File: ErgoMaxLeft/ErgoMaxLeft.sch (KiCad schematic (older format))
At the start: 92 parts, among them J1 AudioJack4_Ground, K1 KEYSW, K10 KEYSW, K11 KEYSW, K12 KEYSW, K13 KEYSW, K14 KEYSW, K15 KEYSW, K16 KEYSW, K17 KEYSW, K18 KEYSW, K19 KEYSW, K2 KEYSW, K20 KEYSW, K21 KEYSW, K22 KEYSW, K23 KEYSW, K24 KEYSW, K25 KEYSW, K26 KEYSW, K27 KEYSW, K28 KEYSW, K29 KEYSW, K3 KEYSW, K30 KEYSW, K31 KEYSW, K32 KEYSW, K33 KEYSW, K34 KEYSW, K35 KEYSW, K36 KEYSW, K37 KEYSW, K38 KEYSW, K39 KEYSW, K4 KEYSW, K40 KEYSW, K41 KEYSW, K42 KEYSW, K43 KEYSW, K44 KEYSW, K5 KEYSW, K6 KEYSW, K7 KEYSW, K8 KEYSW, K9 KEYSW, U1 ProMicro

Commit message: WIP PCB - update diodes footprints to something more accurate, displayed in the proper direction
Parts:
- D1, D10, D11, D12, D13, D14, D15, D16, D17, D18, D19, D2, D20, D21, D22, D23, D24, D25, D26, D27, D28, D29, D3, D30, D31, D32, D33, D34, D35, D36, D37, D38, D39, D4, D40, D41, D42, D43, D44, D5, D6, D7, D8, D9: footprint Keebio-Parts:Diode -> Keebio-Parts:Diode_Long
- J1: footprint Keebio-Parts:4pin35mmAudio -> keyboard_parts:4pin35mmAudio

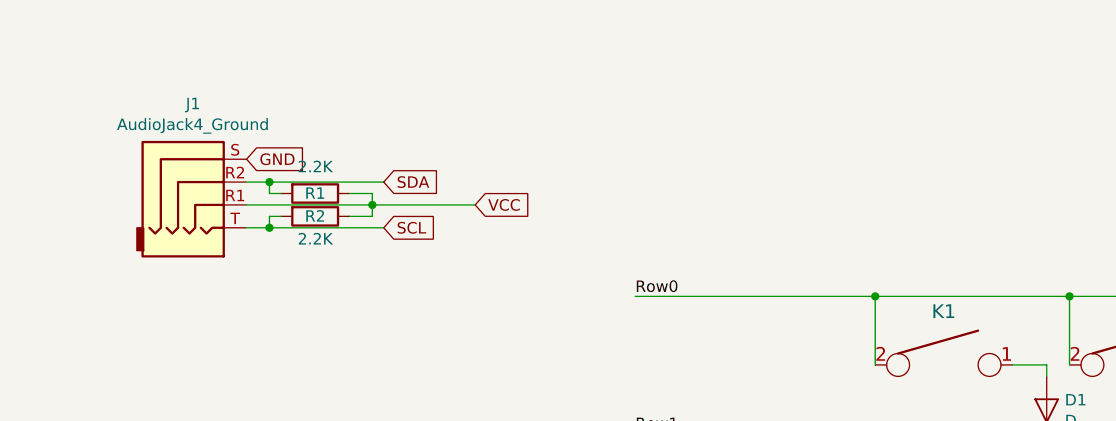
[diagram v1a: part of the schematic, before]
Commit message: WIP PCB - replace jack connector in schematics and PCB to something that actually works properly
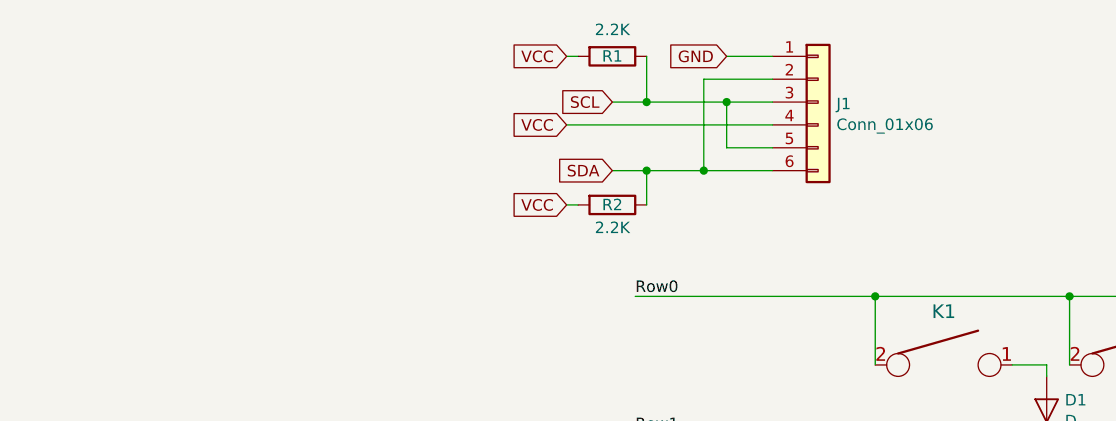
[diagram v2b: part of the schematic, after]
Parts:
- removed J1: AudioJack4_Ground, keyboard_parts:4pin35mmAudio, symbol Connector:AudioJack4_Ground
- added J1: Conn_01x06, Keebio-Parts:4pin35mmAudio, symbol Connector_Generic:Conn_01x06
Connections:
- net GND: now also J1.1 (Pin_1)
- net SCL: now also R1.1, J1.3 (Pin_3), J1.5 (Pin_5); no longer R2.2
- net SDA: now also R2.1, J1.2 (Pin_2), J1.6 (Pin_6); no longer R1.2
- net VCC: now also R1.2, R2.2, J1.4 (Pin_4); no longer R1.1, R2.1
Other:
- moved on the sheet: R1, R2
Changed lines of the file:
@@
-$EndComp
-$Comp
-L Connector:AudioJack4_Ground J1
-U 1 1 5BE696F3
-P 1750 1250
-F 0 "J1" H 1716 1592 50  0000 C CNN
-F 1 "AudioJack4_Ground" H 1716 1501 50  0000 C CNN
-F 2 "keyboard_parts:4pin35mmAudio" H 1750 1250 50  0001 C CNN
-F 3 "~" H 1750 1250 50  0001 C CNN
-	1    1750 1250
-	1    0    0    -1
 $EndComp
 $Comp
@@
 Text GLabel 2650 2750 2    50   Input ~ 0
 GND
-Text GLabel 1950 1150 2    50   Input ~ 0
-GND
 Text GLabel 2650 2950 2    50   Input ~ 0
-VCC
-Text GLabel 2950 1350 2    50   Input ~ 0
 VCC
 Text GLabel 1250 3050 0    50   Input ~ 0
 SDA
-Text GLabel 2550 1250 2    50   Input ~ 0
-SDA
 Text GLabel 1250 3150 0    50   Input ~ 0
 SCL
-Text GLabel 2550 1450 2    50   Input ~ 0
-SCL
 $Comp
 L Device:R R1
 U 1 1 5C270960
-P 2250 1300
-F 0 "R1" V 2250 1300 50  0000 C CNN
-F 1 "2.2K" V 2134 1300 50  0000 C CNN
-F 2 "Keebio-Parts:Resistor" V 2180 1300 50  0001 C CNN
-F 3 "~" H 2250 1300 50  0001 C CNN
-	1    2250 1300
+P 3550 700
+F 0 "R1" V 3550 700 50  0000 C CNN
+F 1 "2.2K" V 3434 700 50  0000 C CNN
+F 2 "Keebio-Parts:Resistor" V 3480 700 50  0001 C CNN
+F 3 "~" H 3550 700 50  0001 C CNN
+	1    3550 700
 	0    1    1    0
 $EndComp
@@
 L Device:R R2
 U 1 1 5C270B6B
-P 2250 1400
-F 0 "R2" V 2250 1400 50  0000 C CNN
-F 1 "2.2K" V 2350 1400 50  0000 C CNN
-F 2 "Keebio-Parts:Resistor" V 2180 1400 50  0001 C CNN
-F 3 "~" H 2250 1400 50  0001 C CNN
-	1    2250 1400
+P 3550 1350
+F 0 "R2" V 3550 1350 50  0000 C CNN
+F 1 "2.2K" V 3650 1350 50  0000 C CNN
+F 2 "Keebio-Parts:Resistor" V 3480 1350 50  0001 C CNN
+F 3 "~" H 3550 1350 50  0001 C CNN
+	1    3550 1350
 	0    1    1    0
 $EndComp
-Wire Wire Line
-	2550 1250 2050 1250
-Wire Wire Line
-	2550 1450 2050 1450
-Wire Wire Line
-	2950 1350 2500 1350
-Wire Wire Line
-	2500 1350 2500 1300
-Wire Wire Line
-	2500 1300 2400 1300
-Connection ~ 2500 1350
-Wire Wire Line
-	2500 1350 1950 1350
-Wire Wire Line
-	2100 1300 2050 1300
-Wire Wire Line
-	2050 1300 2050 1250
-Connection ~ 2050 1250
-Wire Wire Line
-	2050 1250 1950 1250
-Wire Wire Line
-	2400 1400 2500 1400
-Wire Wire Line
-	2500 1400 2500 1350
-Wire Wire Line
-	2100 1400 2050 1400
-Wire Wire Line
-	2050 1400 2050 1450
-Connection ~ 2050 1450
-Wire Wire Line
-	2050 1450 1950 1450
 Text Label 4600 5800 0    50   ~ 0
 Col0
@@
 Wire Wire Line
 	5450 2400 5450 3000
+$Comp
+L Connector_Generic:Conn_01x06 J1
+U 1 1 5BFE26B0
+P 4450 900
+F 0 "J1" H 4530 892 50  0000 L CNN
+F 1 "Conn_01x06" H 4530 801 50  0000 L CNN
+F 2 "Keebio-Parts:4pin35mmAudio" H 4450 900 50  0001 C CNN
+F 3 "~" H 4450 900 50  0001 C CNN
+	1    4450 900
+	1    0    0    -1
+$EndComp
+Text GLabel 3550 1200 0    50   Input ~ 0
+SDA
+Text GLabel 3550 900  0    50   Input ~ 0
+SCL
+Text GLabel 3350 700  0    50   Input ~ 0
+VCC
+Text GLabel 3350 1350 0    50   Input ~ 0
+VCC
+Wire Wire Line
+	3550 1200 3700 1200
+Wire Wire Line
+	4250 800  3950 800
+Wire Wire Line
+	3950 800  3950 1200
+Connection ~ 3950 1200
+Wire Wire Line
+	3950 1200 4250 1200
+Wire Wire Line
+	4250 900  4050 900
+Wire Wire Line
+	4250 1100 4050 1100
+Wire Wire Line
+	4050 1100 4050 900
+Connection ~ 4050 900
+Wire Wire Line
+	4050 900  3700 900
+Wire Wire Line
+	3700 700  3700 900
+Connection ~ 3700 900
+Wire Wire Line
+	3700 900  3550 900
+Wire Wire Line
+	3350 1350 3400 1350
+Wire Wire Line
+	3350 700  3400 700
+Wire Wire Line
+	3700 1350 3700 1200
+Connection ~ 3700 1200
+Wire Wire Line
+	3700 1200 3950 1200
+Text GLabel 4050 700  0    50   Input ~ 0
+GND
+Text GLabel 3350 1000 0    50   Input ~ 0
+VCC
+Wire Wire Line
+	3350 1000 4250 1000
+Wire Wire Line
+	4050 700  4250 700
 $EndSCHEMATC

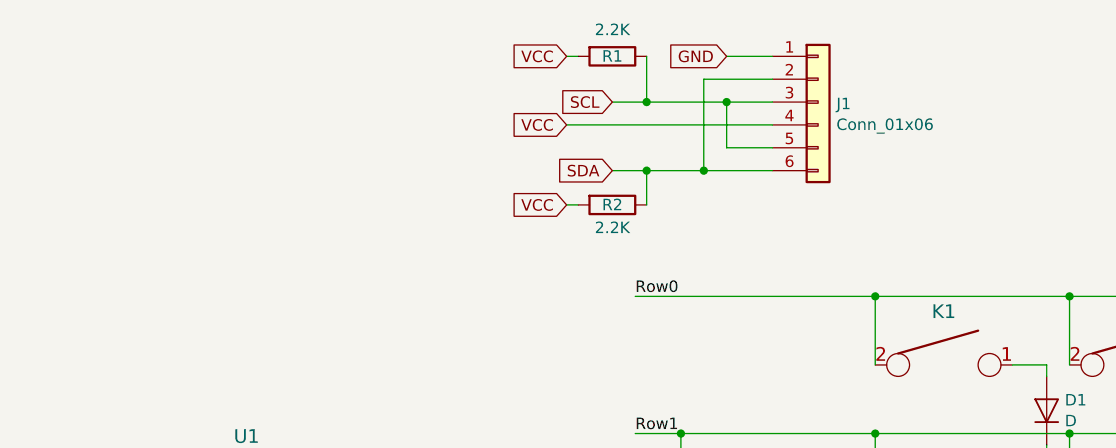
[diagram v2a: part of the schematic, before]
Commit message: Change Jack 3.5 connector to PJ-320A model 4 pins
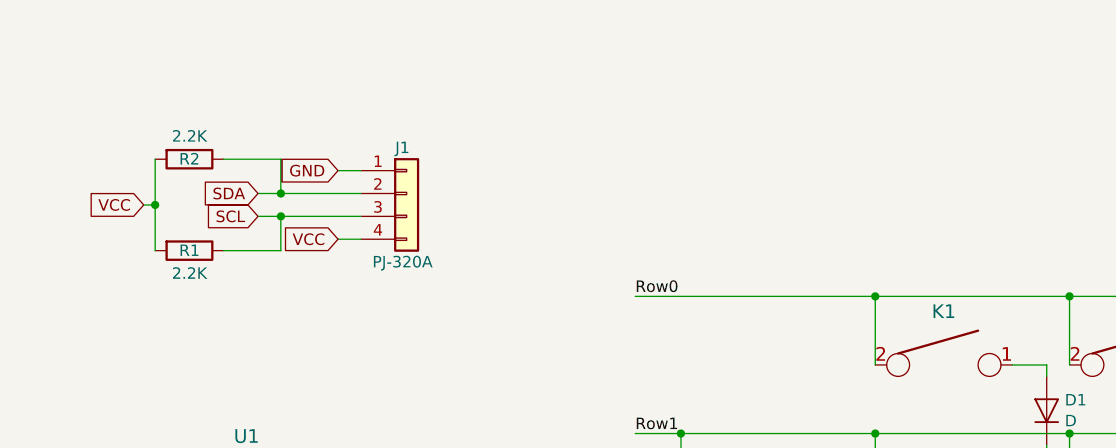
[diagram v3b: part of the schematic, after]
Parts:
- removed J1: Conn_01x06, Keebio-Parts:4pin35mmAudio, symbol Connector_Generic:Conn_01x06
- added J1: PJ-320A, Keebio-Parts:TRRS-PJ-320A-no-Fmask, symbol Connector_Generic:Conn_01x04
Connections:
- net GND: now also J1.1 (Pin_1)
- net SCL: now also J1.3 (Pin_3)
- net SDA: now also J1.2 (Pin_2)
- net VCC: now also J1.4 (Pin_4)
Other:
- moved on the sheet: R1, R2
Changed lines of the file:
@@
 L Device:R R1
 U 1 1 5C270960
-P 3550 700
-F 0 "R1" V 3550 700 50  0000 C CNN
-F 1 "2.2K" V 3434 700 50  0000 C CNN
-F 2 "Keebio-Parts:Resistor" V 3480 700 50  0001 C CNN
-F 3 "~" H 3550 700 50  0001 C CNN
-	1    3550 700
+P 1700 1550
+F 0 "R1" V 1700 1550 50  0000 C CNN
+F 1 "2.2K" V 1800 1550 50  0000 C CNN
+F 2 "Keebio-Parts:Resistor" V 1630 1550 50  0001 C CNN
+F 3 "~" H 1700 1550 50  0001 C CNN
+	1    1700 1550
 	0    1    1    0
 $EndComp
@@
 L Device:R R2
 U 1 1 5C270B6B
-P 3550 1350
-F 0 "R2" V 3550 1350 50  0000 C CNN
-F 1 "2.2K" V 3650 1350 50  0000 C CNN
-F 2 "Keebio-Parts:Resistor" V 3480 1350 50  0001 C CNN
-F 3 "~" H 3550 1350 50  0001 C CNN
-	1    3550 1350
+P 1700 1150
+F 0 "R2" V 1700 1150 50  0000 C CNN
+F 1 "2.2K" V 1600 1150 50  0000 C CNN
+F 2 "Keebio-Parts:Resistor" V 1630 1150 50  0001 C CNN
+F 3 "~" H 1700 1150 50  0001 C CNN
+	1    1700 1150
 	0    1    1    0
 $EndComp
@@
 Wire Wire Line
 	5450 2400 5450 3000
+Text GLabel 2000 1300 0    50   Input ~ 0
+SDA
+Text GLabel 2000 1400 0    50   Input ~ 0
+SCL
+Text GLabel 2350 1500 0    50   Input ~ 0
+VCC
+Text GLabel 1500 1350 0    50   Input ~ 0
+VCC
+Wire Wire Line
+	1500 1350 1550 1350
+Text GLabel 2350 1200 0    50   Input ~ 0
+GND
 $Comp
-L Connector_Generic:Conn_01x06 J1
-U 1 1 5BFE26B0
-P 4450 900
-F 0 "J1" H 4530 892 50  0000 L CNN
-F 1 "Conn_01x06" H 4530 801 50  0000 L CNN
-F 2 "Keebio-Parts:4pin35mmAudio" H 4450 900 50  0001 C CNN
-F 3 "~" H 4450 900 50  0001 C CNN
-	1    4450 900
+L Connector_Generic:Conn_01x04 J1
+U 1 1 5BEF69BF
+P 2650 1300
+F 0 "J1" H 2600 1500 50  0000 L CNN
+F 1 "PJ-320A" H 2500 1000 50  0000 L CNN
+F 2 "Keebio-Parts:TRRS-PJ-320A-no-Fmask" H 2650 1300 50  0001 C CNN
+F 3 "~" H 2650 1300 50  0001 C CNN
+	1    2650 1300
 	1    0    0    -1
 $EndComp
-Text GLabel 3550 1200 0    50   Input ~ 0
-SDA
-Text GLabel 3550 900  0    50   Input ~ 0
-SCL
-Text GLabel 3350 700  0    50   Input ~ 0
-VCC
-Text GLabel 3350 1350 0    50   Input ~ 0
-VCC
 Wire Wire Line
-	3550 1200 3700 1200
+	2000 1400 2100 1400
 Wire Wire Line
-	4250 800  3950 800
+	2000 1300 2100 1300
 Wire Wire Line
-	3950 800  3950 1200
-Connection ~ 3950 1200
+	1850 1150 2100 1150
 Wire Wire Line
-	3950 1200 4250 1200
+	2100 1150 2100 1300
 Wire Wire Line
-	4250 900  4050 900
+	1850 1550 2100 1550
 Wire Wire Line
-	4250 1100 4050 1100
+	2100 1550 2100 1400
 Wire Wire Line
-	4050 1100 4050 900
-Connection ~ 4050 900
+	1550 1350 1550 1150
 Wire Wire Line
-	4050 900  3700 900
+	1550 1350 1550 1550
+Connection ~ 1550 1350
 Wire Wire Line
-	3700 700  3700 900
-Connection ~ 3700 900
+	2350 1200 2450 1200
 Wire Wire Line
-	3700 900  3550 900
+	2100 1300 2450 1300
+Connection ~ 2100 1300
 Wire Wire Line
-	3350 1350 3400 1350
+	2100 1400 2450 1400
+Connection ~ 2100 1400
 Wire Wire Line
-	3350 700  3400 700
-Wire Wire Line
-	3700 1350 3700 1200
-Connection ~ 3700 1200
-Wire Wire Line
-	3700 1200 3950 1200
-Text GLabel 4050 700  0    50   Input ~ 0
-GND
-Text GLabel 3350 1000 0    50   Input ~ 0
-VCC
-Wire Wire Line
-	3350 1000 4250 1000
-Wire Wire Line
-	4050 700  4250 700
+	2350 1500 2450 1500
 $EndSCHEMATC

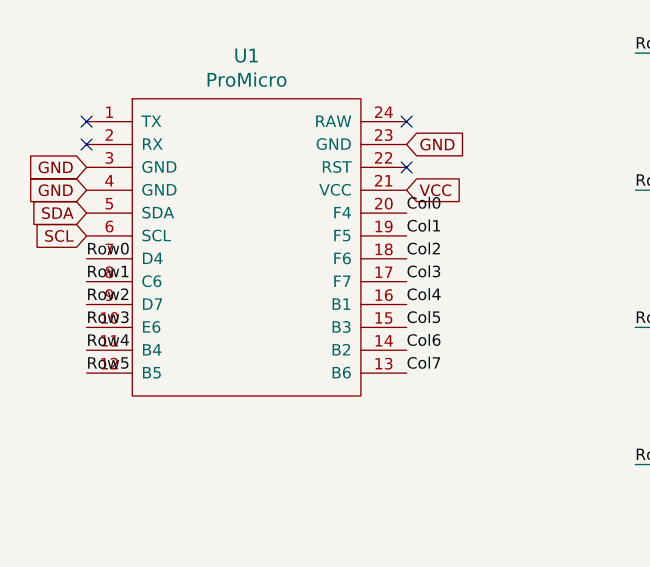
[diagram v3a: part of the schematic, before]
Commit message: Re-work pro mini pinout for better wiring on PCB and finish PCB wiring
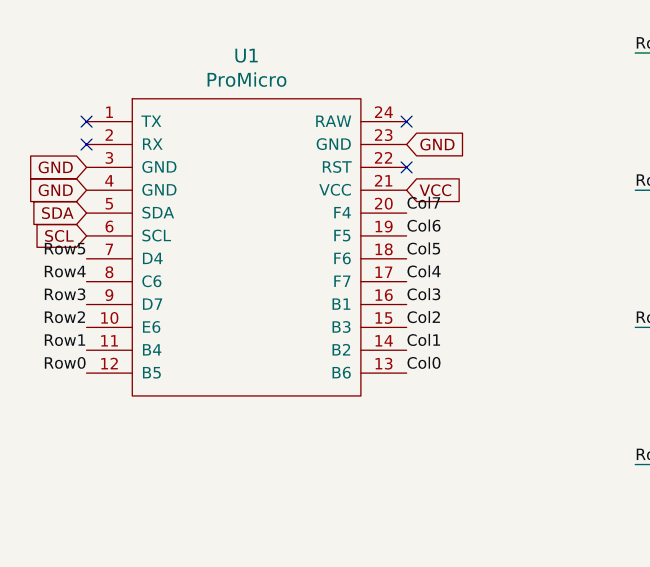
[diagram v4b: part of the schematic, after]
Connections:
- net Col0: now also U1.13 (B6); no longer U1.20 (F4)
- net Col1: now also U1.14 (B2); no longer U1.19 (F5)
- net Col2: now also U1.15 (B3); no longer U1.18 (F6)
- net Col3: now also U1.16 (B1); no longer U1.17 (F7)
- net Col4: now also U1.17 (F7); no longer U1.16 (B1)
- net Col5: now also U1.18 (F6); no longer U1.15 (B3)
- net Col6: now also U1.19 (F5); no longer U1.14 (B2)
- net Col7: now also U1.20 (F4); no longer U1.13 (B6)
- net Row0: now also U1.12 (B5); no longer U1.7 (D4)
- net Row1: now also U1.11 (B4); no longer U1.8 (C6)
- net Row2: now also U1.10 (E6); no longer U1.9 (D7)
- net Row3: now also U1.9 (D7); no longer U1.10 (E6)
- net Row4: now also U1.8 (C6); no longer U1.11 (B4)
- net Row5: now also U1.7 (D4); no longer U1.12 (B5)
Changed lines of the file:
@@
 Text Label 3650 4750 0    50   ~ 0
 Row5
-Text Label 1250 3250 0    50   ~ 0
+Text Label 1250 3250 2    50   ~ 0
+Row5
+Text Label 1250 3350 2    50   ~ 0
+Row4
+Text Label 1250 3450 2    50   ~ 0
+Row3
+Text Label 1250 3550 2    50   ~ 0
+Row2
+Text Label 1250 3650 2    50   ~ 0
+Row1
+Text Label 1250 3750 2    50   ~ 0
 Row0
-Text Label 1250 3350 0    50   ~ 0
-Row1
-Text Label 1250 3450 0    50   ~ 0
-Row2
-Text Label 1250 3550 0    50   ~ 0
-Row3
-Text Label 1250 3650 0    50   ~ 0
-Row4
-Text Label 1250 3750 0    50   ~ 0
-Row5
 Text Label 2650 3750 0    50   ~ 0
+Col0
+Text Label 2650 3650 0    50   ~ 0
+Col1
+Text Label 2650 3550 0    50   ~ 0
+Col2
+Text Label 2650 3450 0    50   ~ 0
+Col3
+Text Label 2650 3350 0    50   ~ 0
+Col4
+Text Label 2650 3250 0    50   ~ 0
+Col5
+Text Label 2650 3150 0    50   ~ 0
+Col6
+Text Label 2650 3050 0    50   ~ 0
 Col7
-Text Label 2650 3650 0    50   ~ 0
-Col6
-Text Label 2650 3550 0    50   ~ 0
-Col5
-Text Label 2650 3450 0    50   ~ 0
-Col4
-Text Label 2650 3350 0    50   ~ 0
-Col3
-Text Label 2650 3250 0    50   ~ 0
-Col2
-Text Label 2650 3150 0    50   ~ 0
-Col1
-Text Label 2650 3050 0    50   ~ 0
-Col0
 NoConn ~ 1250 2650
 NoConn ~ 1250 2750
